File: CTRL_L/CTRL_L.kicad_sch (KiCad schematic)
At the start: 22 parts, among them J1 BM14B-NSHSS-TBT_LF__SN_, J2 BM04B-NSHSS-TBT_LF__SN_, J3 BM04B-NSHSS-TBT_LF__SN_, J4 5051100592, U1 74LVC1G08

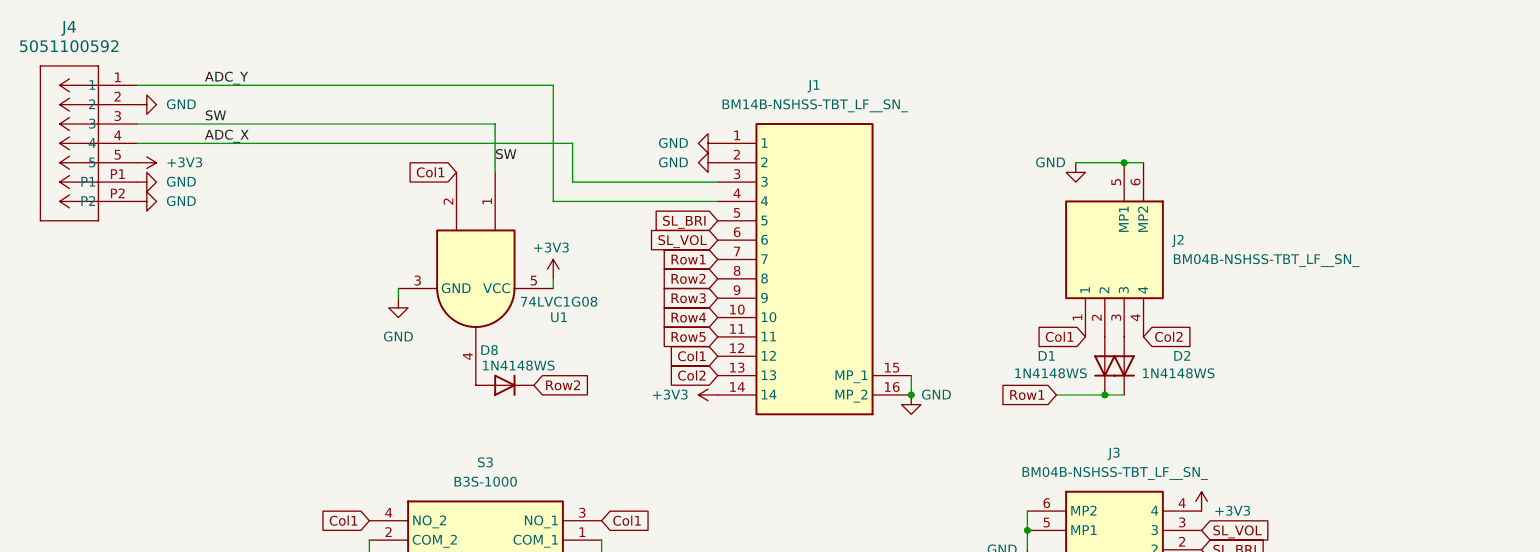
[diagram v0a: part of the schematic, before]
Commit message: CTRL_L Cleanup: Reduced 14 to 12 pins, added Ground Planes and Vias, and general wiring cleanups
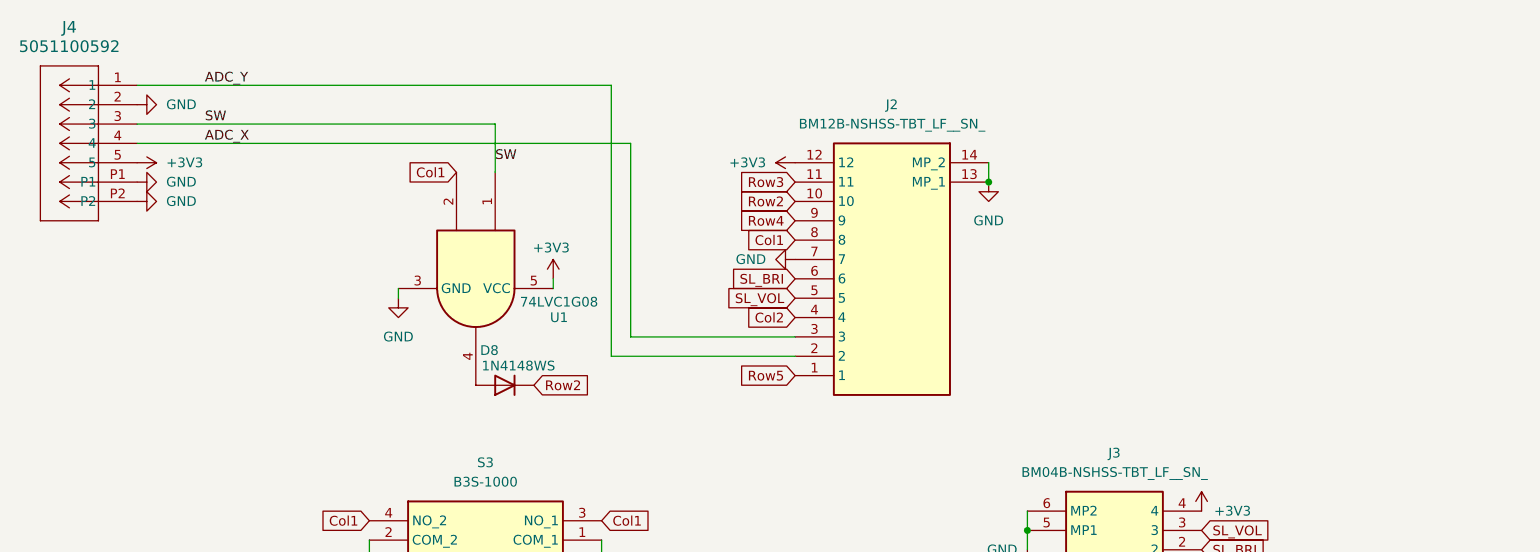
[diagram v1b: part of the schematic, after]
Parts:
- removed D1, D2: 1N4148WS, Diode_SMD:D_SOD-323, symbol Diode:1N4148WS
- removed J1: BM14B-NSHSS-TBT_LF__SN_, BM14B-NSHSS-TBT:BM14BNSHSSTBTLFSN, symbol BM14B-NSHSS-TBT_LF__SN_:BM14B-NSHSS-TBT_LF__SN_
- removed J2: BM04B-NSHSS-TBT_LF__SN_, BM04B-NSHSS-TBT:BM04BNSHSSTBTLFSN, symbol BM04B-NSHSS-TBT_LF__SN_:BM04B-NSHSS-TBT_LF__SN_
- added J2: BM12B-NSHSS-TBT_LF__SN_, BM12BNSHSSTBTLFSN, symbol BM12B-NSHSS-TBT_LF__SN_:BM12B-NSHSS-TBT_LF__SN_
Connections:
- net +3V3: now also J2.12
- net ADC_X: now also J2.3
- net ADC_Y: now also J2.2
- net Col1: now also J2.8
- net Col2: now also J2.4
- net GND: now also J2.13 (MP_1), J2.14 (MP_2), J2.7
- net Row2: now also J2.10
- net Row3: now also J2.11
- net Row4: now also J2.9
- net Row5: now also J2.1
- net SL_BRI: now also J2.6
- net SL_VOL: now also J2.5

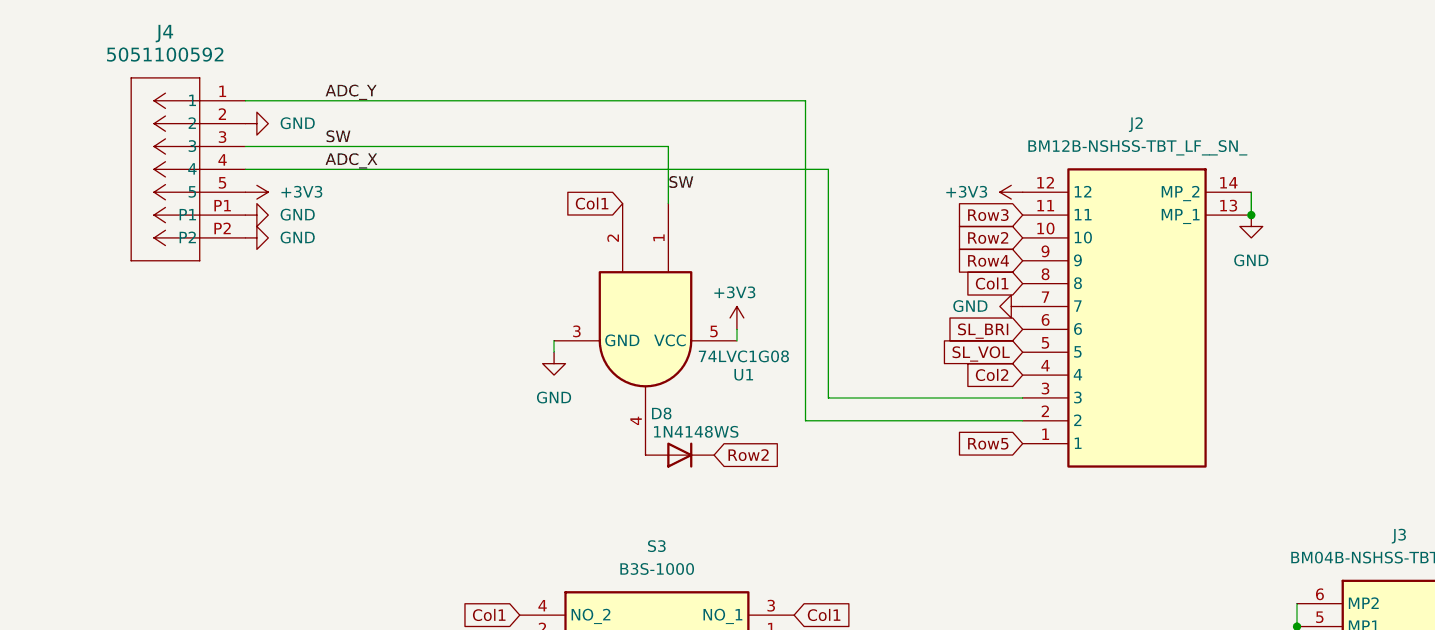
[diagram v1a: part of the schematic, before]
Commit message: Bottom Screen fully Wired!
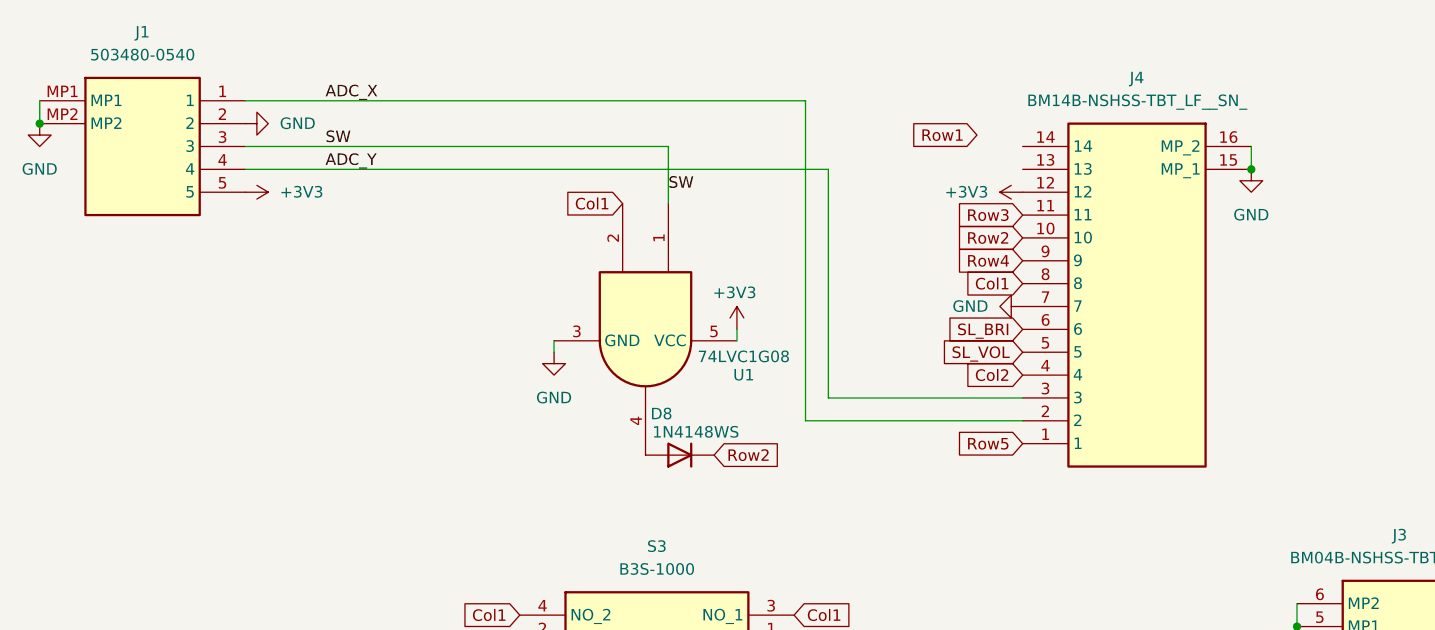
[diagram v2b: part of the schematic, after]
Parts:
- removed J2: BM12B-NSHSS-TBT_LF__SN_, BM12BNSHSSTBTLFSN, symbol BM12B-NSHSS-TBT_LF__SN_:BM12B-NSHSS-TBT_LF__SN_
- removed J4: 5051100592, 5051100592:CON_5051100592_MOL, symbol 5051100592:5051100592
- added J1: 503480-0540, 5034800540, symbol 503480-0540:503480-0540
- added J4: BM14B-NSHSS-TBT_LF__SN_, BM14BNSHSSTBTLFSN, symbol BM14B-NSHSS-TBT_LF__SN_:BM14B-NSHSS-TBT_LF__SN_
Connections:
- net +3V3: now also J1.5, J4.12
- net ADC_X: now also J1.1, J4.2
- net ADC_Y: now also J1.4, J4.3
- net Col1: now also J4.8
- net Col2: now also J4.4
- net GND: now also J1.2, J1.MP1, J1.MP2, J4.15 (MP_1), J4.16 (MP_2), J4.7
- net Row2: now also J4.10
- net Row3: now also J4.11
- net Row4: now also J4.9
- net Row5: now also J4.1
- net SL_BRI: now also J4.6
- net SL_VOL: now also J4.5
- net SW: now also J1.3

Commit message: Corrected CTRL_PWR (+other WIP changes)
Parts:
- added U2: DRV5033FAxDBZ, Package_TO_SOT_SMD:SOT-23, symbol Sensor_Magnetic:DRV5033FAxDBZ
- J3: now not fitted; now left out of the parts list
- J4: footprint BM14BNSHSSTBTLFSN -> BM14B-NSHSS-TBT:BM14BNSHSSTBTLFSN
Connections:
- net +3V3: now also U2.1 (VCC)
- net GND: now also U2.3 (GND)
- net Row1: now also J4.13
- net HALL: now reaches J4.14
- net HALL: now also U2.2 (OUT)

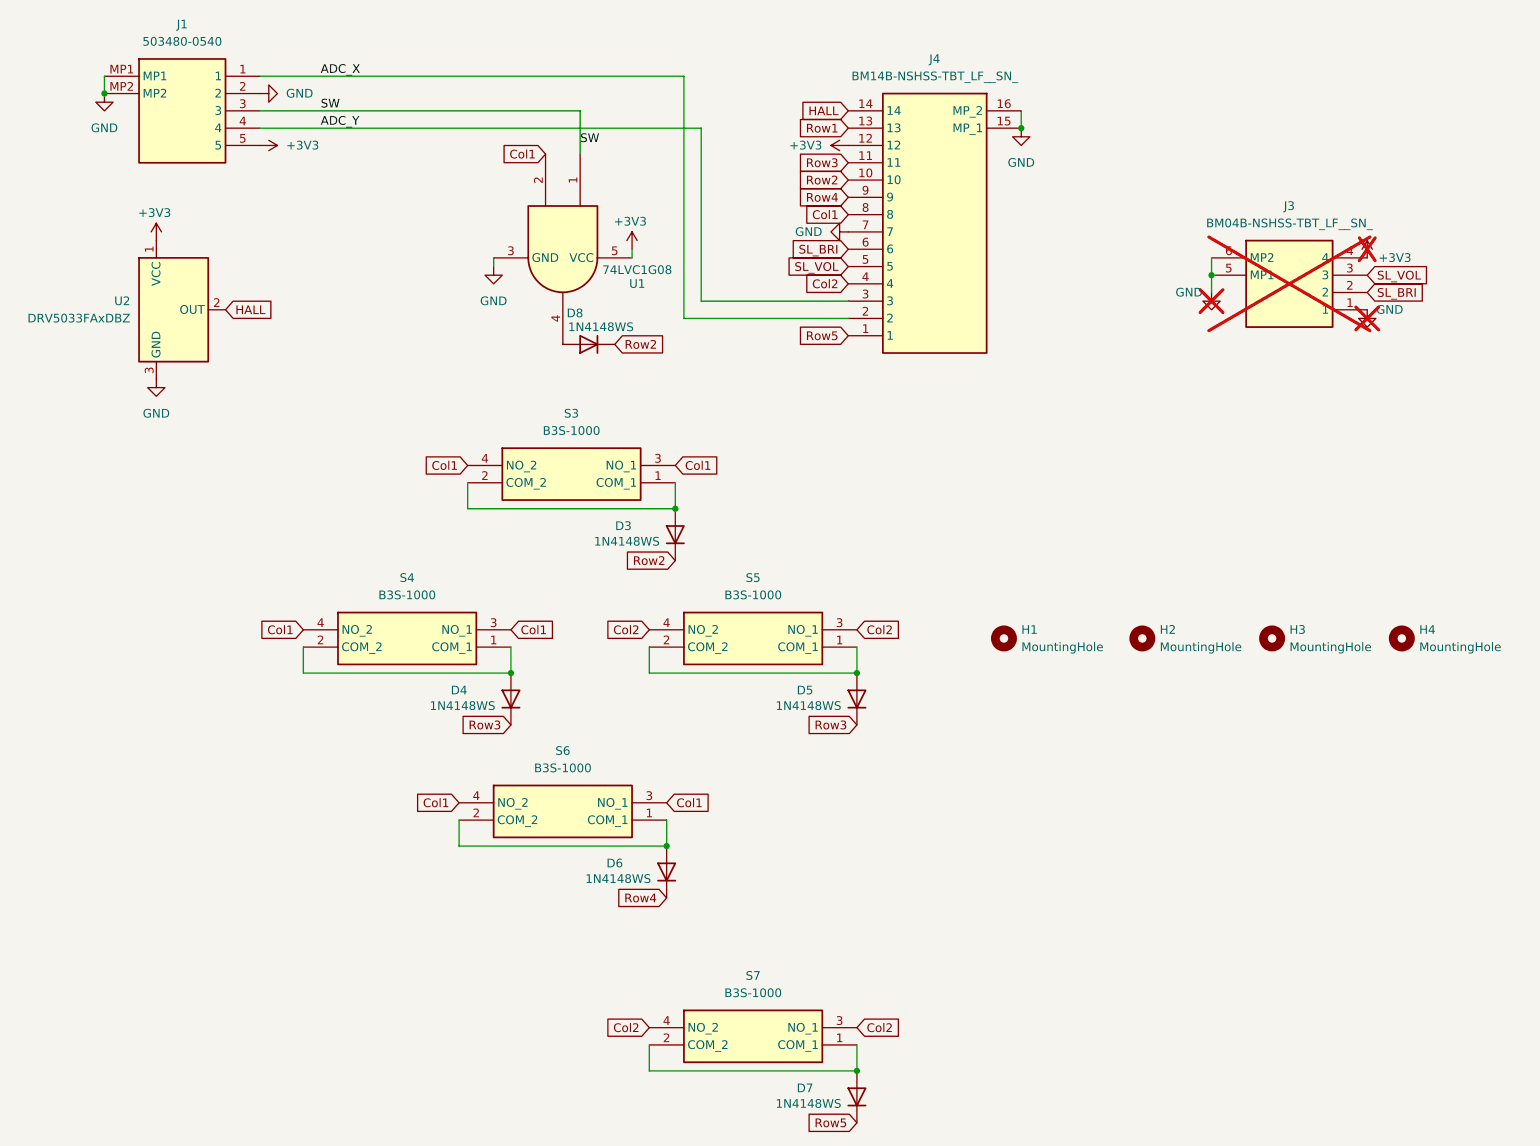
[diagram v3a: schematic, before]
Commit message: Added ESD Diodes to CTRL_L.
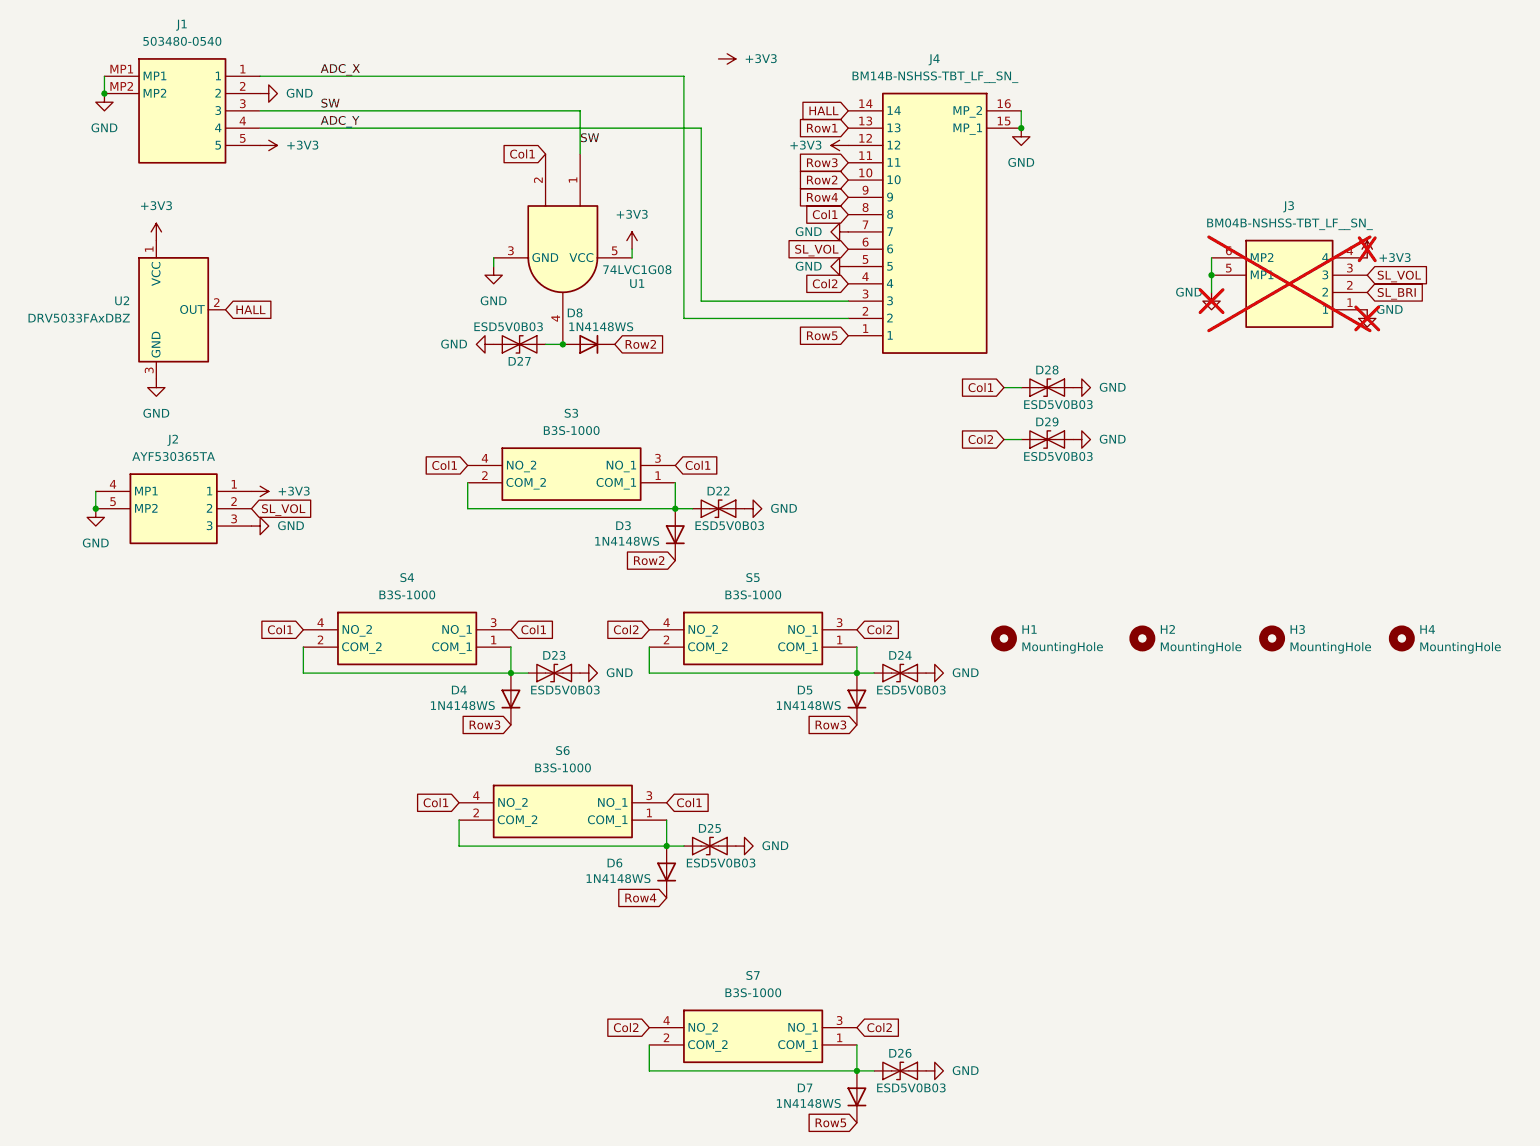
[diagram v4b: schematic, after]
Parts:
- added D22, D23, D24, D25, D26, D27, D28, D29: ESD5V0B03, A_HDJ_Library:D_0402_1005Metric, symbol Diode:ESD9B5.0ST5G
- added J2: AYF530365TA, AYF530365TA:AYF530365T, symbol AYF530365TA:AYF530365TA
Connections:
- net +3V3: now also J2.1
- net Col1: now also D28.2 (A2)
- net Col2: now also D29.2 (A2)
- net GND: now also J4.5, D22.1 (A1), D23.1 (A1), D24.1 (A1), D25.1 (A1), D26.1 (A1), D27.1 (A1), D28.1 (A1), D29.1 (A1), J2.3, J2.4 (MP1), J2.5 (MP2)
- net SL_BRI: no longer J4.6
- net SL_VOL: now also J4.6, J2.2; no longer J4.5
- net at D5.2 (A), S5.1 (COM_1), S5.2 (COM_2): now also D24.2 (A2)
- net at D4.2 (A), S4.1 (COM_1), S4.2 (COM_2): now also D23.2 (A2)
- net at D6.2 (A), S6.1 (COM_1), S6.2 (COM_2): now also D25.2 (A2)
- net at D7.2 (A), S7.1 (COM_1), S7.2 (COM_2): now also D26.2 (A2)
- net at D8.2 (A), U1.4: now also D27.2 (A2)
- net at D3.2 (A), S3.1 (COM_1), S3.2 (COM_2): now also D22.2 (A2)

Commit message: Updated CTRL_L to use FPC connectors, single volume slider, extra connector for CTRL_Z and added ESD Diodes.
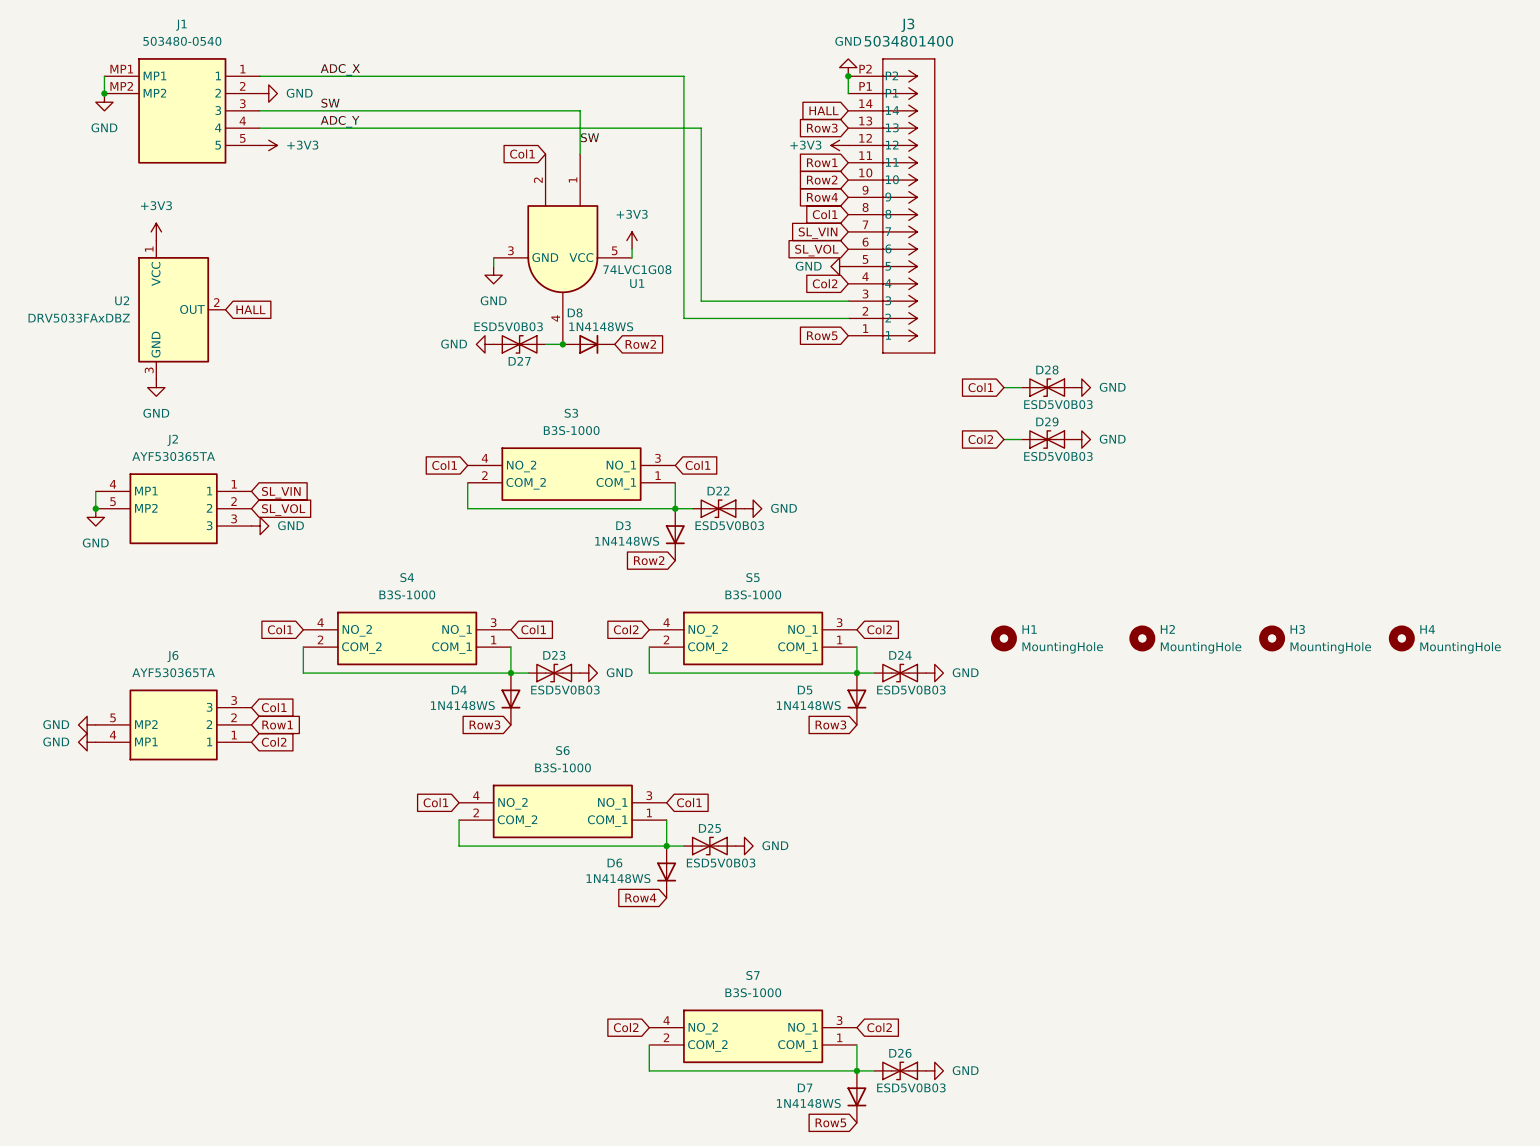
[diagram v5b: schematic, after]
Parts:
- removed J3: BM04B-NSHSS-TBT_LF__SN_, BM04B-NSHSS-TBT:BM04BNSHSSTBTLFSN, symbol BM04B-NSHSS-TBT_LF__SN_:BM04B-NSHSS-TBT_LF__SN_
- removed J4: BM14B-NSHSS-TBT_LF__SN_, BM14B-NSHSS-TBT:BM14BNSHSSTBTLFSN, symbol BM14B-NSHSS-TBT_LF__SN_:BM14B-NSHSS-TBT_LF__SN_
- added J3: 5034801400, 5034801400:5034801400, symbol 5034801400:5034801400
- added J6: AYF530365TA, AYF530365TA:AYF530365T, symbol AYF530365TA:AYF530365TA
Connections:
- net +3V3: now also J3.12; no longer J2.1
- net ADC_X: now also J3.2
- net ADC_Y: now also J3.3
- net Col1: now also J3.8, J6.3
- net Col2: now also J3.4, J6.1
- net GND: now also J3.5, J3.P1, J3.P2, J6.4 (MP1), J6.5 (MP2)
- net HALL: now also J3.14
- net Row1: now also J3.11, J6.2
- net Row2: now also J3.10
- net Row3: now also J3.13
- net Row4: now also J3.9
- net Row5: now also J3.1
- net SL_VOL: now also J3.6
- new net SL_VIN: J2.1, J3.7
